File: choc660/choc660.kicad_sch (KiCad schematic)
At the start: 7 parts

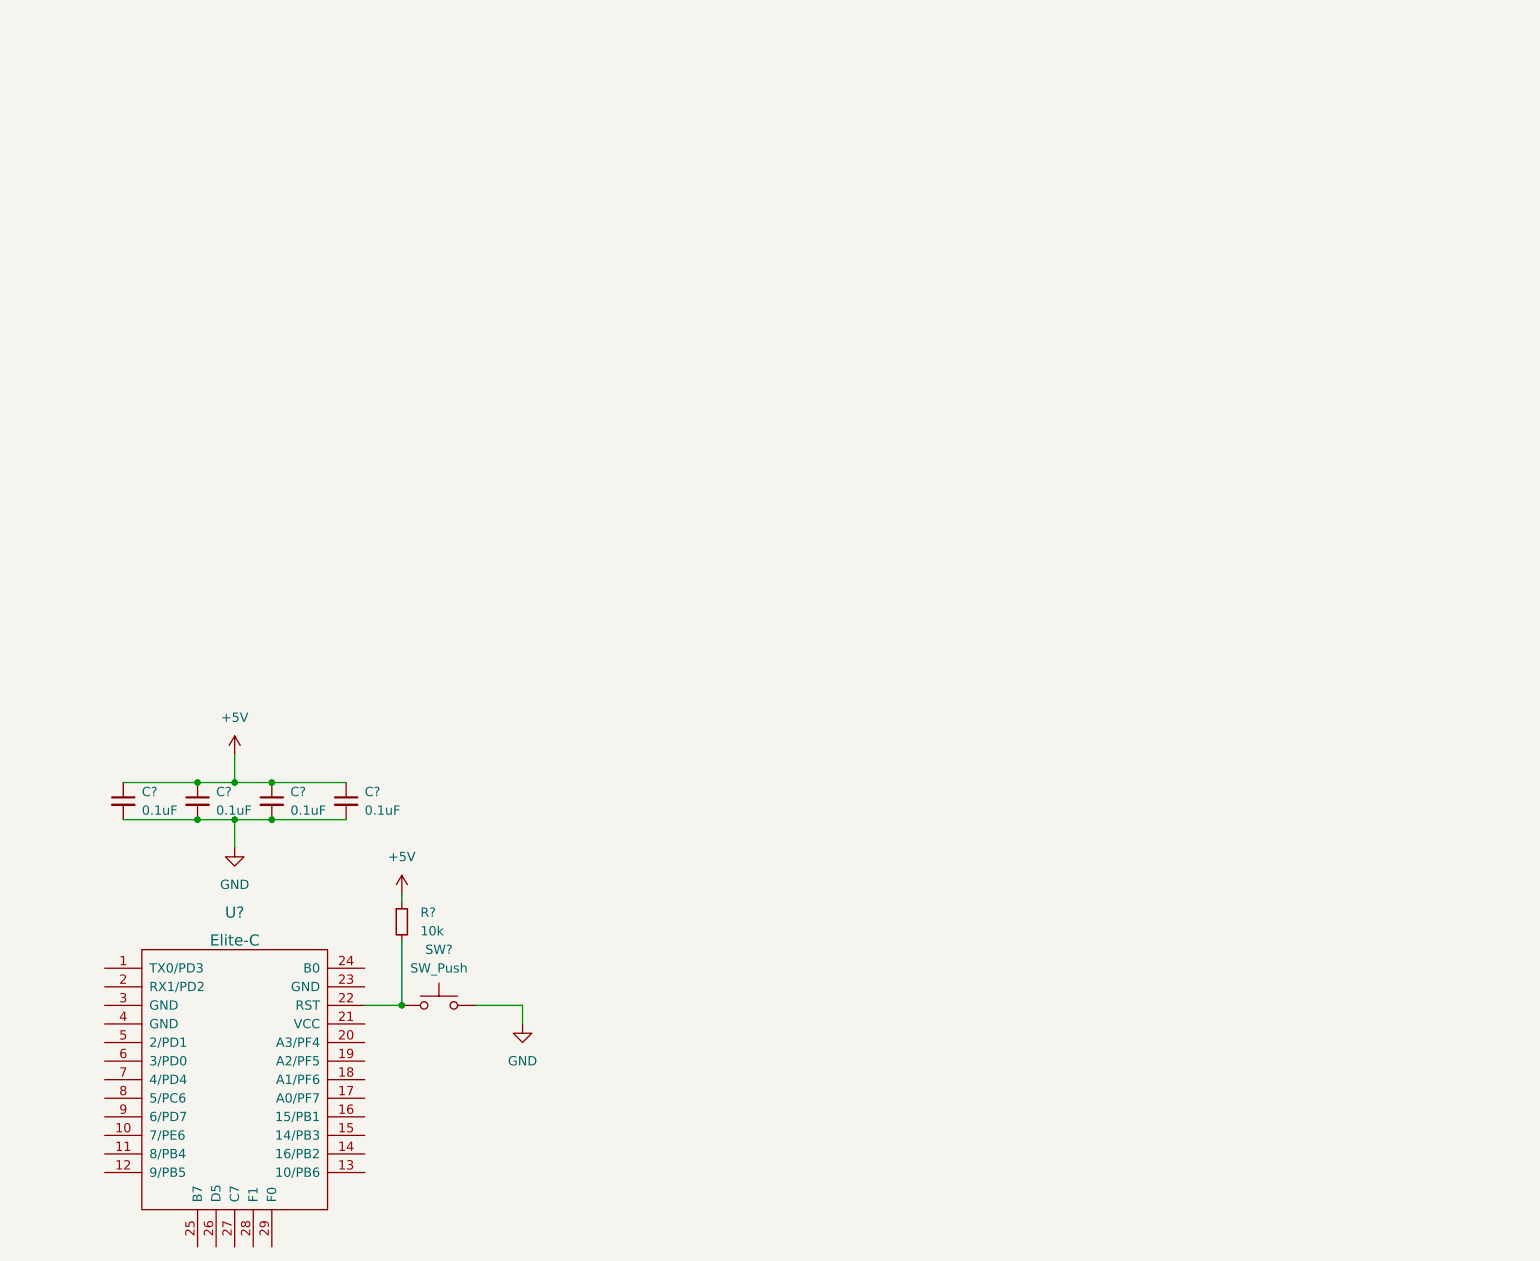
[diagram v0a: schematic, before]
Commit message: set up switch grid, drop reset switch and caps
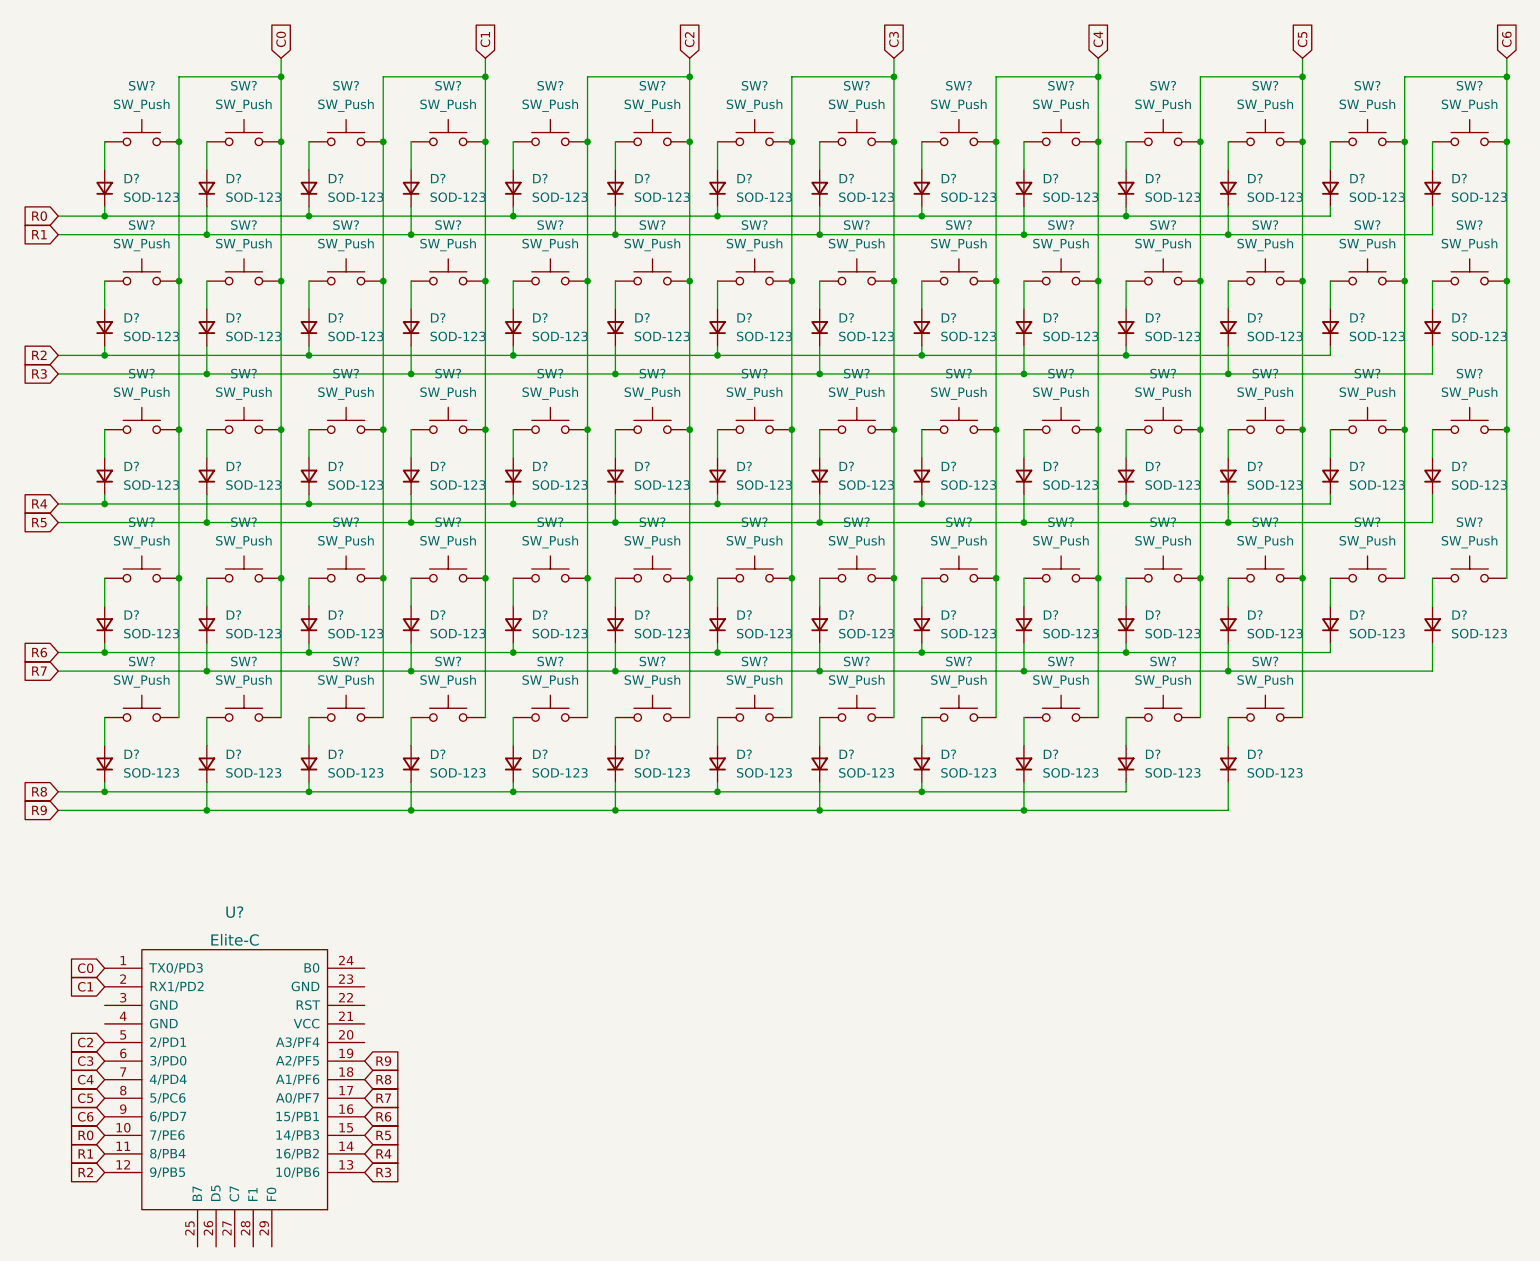
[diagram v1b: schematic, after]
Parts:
- removed C? (x4): 0.1uF, symbol Device:C_Small
- removed R?: 10k, symbol Device:R_Small
- removed SW?: SW_Push, symbol Switch:SW_Push
- added D? (x68): SOD-123, symbol Device:D_Small
- added SW? (x68): SW_Push, symbol Switch:SW_Push
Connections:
- net C0: now reaches U?.1 (TX0/PD3)
- net C0: now also SW?.2, SW?.2, SW?.2, SW?.2, SW?.2, SW?.2, SW?.2, SW?.2, SW?.2, SW?.2
- net R0: now reaches U?.10 (7/PE6)
- net R0: now also D?.1 (K), D?.1 (K), D?.1 (K), D?.1 (K), D?.1 (K), D?.1 (K), D?.1 (K)
- net R1: now reaches U?.11 (8/PB4)
- net R1: now also D?.1 (K), D?.1 (K), D?.1 (K), D?.1 (K), D?.1 (K), D?.1 (K), D?.1 (K)
- net R2: now reaches U?.12 (9/PB5)
- net R2: now also D?.1 (K), D?.1 (K), D?.1 (K), D?.1 (K), D?.1 (K), D?.1 (K), D?.1 (K)
- net R3: now reaches U?.13 (10/PB6)
- net R3: now also D?.1 (K), D?.1 (K), D?.1 (K), D?.1 (K), D?.1 (K), D?.1 (K), D?.1 (K)
- net R4: now reaches U?.14 (16/PB2)
- net R4: now also D?.1 (K), D?.1 (K), D?.1 (K), D?.1 (K), D?.1 (K), D?.1 (K), D?.1 (K)
- net R5: now reaches U?.15 (14/PB3)
- net R5: now also D?.1 (K), D?.1 (K), D?.1 (K), D?.1 (K), D?.1 (K), D?.1 (K), D?.1 (K)
- net R6: now reaches U?.16 (15/PB1)
- net R6: now also D?.1 (K), D?.1 (K), D?.1 (K), D?.1 (K), D?.1 (K), D?.1 (K), D?.1 (K)
- net R7: now reaches U?.17 (A0/PF7)
- net R7: now also D?.1 (K), D?.1 (K), D?.1 (K), D?.1 (K), D?.1 (K), D?.1 (K), D?.1 (K)
- net R8: now reaches U?.18 (A1/PF6)
- net R8: now also D?.1 (K), D?.1 (K), D?.1 (K), D?.1 (K), D?.1 (K), D?.1 (K)
- net R9: now reaches U?.19 (A2/PF5)
- net R9: now also D?.1 (K), D?.1 (K), D?.1 (K), D?.1 (K), D?.1 (K), D?.1 (K)
- net C1: now reaches U?.2 (RX1/PD2)
- net C1: now also SW?.2, SW?.2, SW?.2, SW?.2, SW?.2, SW?.2, SW?.2, SW?.2, SW?.2, SW?.2
- net C2: now reaches U?.5 (2/PD1)
- net C2: now also SW?.2, SW?.2, SW?.2, SW?.2, SW?.2, SW?.2, SW?.2, SW?.2, SW?.2, SW?.2
- net C3: now reaches U?.6 (3/PD0)
- net C3: now also SW?.2, SW?.2, SW?.2, SW?.2, SW?.2, SW?.2, SW?.2, SW?.2, SW?.2, SW?.2
- net C4: now reaches U?.7 (4/PD4)
- net C4: now also SW?.2, SW?.2, SW?.2, SW?.2, SW?.2, SW?.2, SW?.2, SW?.2, SW?.2, SW?.2
- net C5: now reaches U?.8 (5/PC6)
- net C5: now also SW?.2, SW?.2, SW?.2, SW?.2, SW?.2, SW?.2, SW?.2, SW?.2, SW?.2, SW?.2
- net C6: now reaches U?.9 (6/PD7)
- net C6: now also SW?.2, SW?.2, SW?.2, SW?.2, SW?.2, SW?.2, SW?.2, SW?.2
- new net: D?.2 (A), SW?.1 (x68)
